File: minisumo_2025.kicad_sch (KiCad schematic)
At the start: 90 parts, among them J1 USB_C Connector, J10 DISTANCE_R90, J11 DISTANCE_R, J12 DISTANCE_RF, J13 DISTANCE_L90, J14 DISTANCE_L, J15 LINE_LEFT, J16 DISTANCE_LF, J2 SERVO, J3 START_MODULE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

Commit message: usb routing
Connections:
- net GPIO15 is gone; now on net DISTANCE_L: U3.8 (IO15)
- net GPIO16 is gone; now on net DISTANCE_L90: U3.9 (IO16)
- net GPIO4 is gone; now on net DISTANCE_R90: U3.4 (IO4)
- net GPIO5 is gone; now on net DISTANCE_R: U3.5 (IO5)
- net GPIO6 is gone; now on net DISTANCE_RF: U3.6 (IO6)
- net GPIO7 is gone; now on net DISTANCE_LF: U3.7 (IO7)
- net LINE_LEFT is gone; now on net GPIO8: R23.1, R24.2
- net LINE_RIGHT is gone; now on net GPIO18: R21.1, R22.2
- net SERVO_PWM is gone; now on net GPIO17: J2.3 (Pin_3)
- net DISTANCE_L: now also U5.2 (A2); no longer U5.8 (A6)
- net DISTANCE_L90: now also U5.1 (A1); no longer U5.9 (A7)
- net DISTANCE_L90_OUT: now also U5.20 (B1); no longer U5.12 (B7)
- net DISTANCE_LF: now also U5.3 (A3); no longer U5.7 (A5)
- net DISTANCE_LF_OUT: now also U5.18 (B3); no longer U5.14 (B5)
- net DISTANCE_L_OUT: now also U5.19 (B2); no longer U5.13 (B6)
- net DISTANCE_R: now also U5.8 (A6); no longer U5.2 (A2)
- net DISTANCE_R90: now also U5.9 (A7); no longer U5.1 (A1)
- net DISTANCE_R90_OUT: now also U5.12 (B7); no longer U5.20 (B1)
- net DISTANCE_RF: now also U5.7 (A5); no longer U5.3 (A3)
- net DISTANCE_RF_OUT: now also U5.14 (B5); no longer U5.18 (B3)
- net DISTANCE_R_OUT: now also U5.13 (B6); no longer U5.19 (B2)
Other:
- note added: "TODO: - maybe make clearance bigger between batt plane and gnd"
- note removed: "TODO: - DO NOT PLACE THE BIG CAPACITORS BETWEEN THE MOTORS, THEY ARE NOT NEEDED"
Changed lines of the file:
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@@
 		)
 	)
-	(text "TODO:\n - DO NOT PLACE THE BIG CAPACITORS BETWEEN THE MOTORS, THEY ARE NOT NEEDED\n\n\n"
+	(text "TODO:\n - maybe make clearance bigger between batt plane and gnd\n\n\n\n"
 		(exclude_from_sim no)
 		(at 290.322 22.606 0)
@@
 		)
 	)
-	(label "DISTANCE_L_OUT"
-		(at 87.63 229.87 180)
-		(effects
-			(font
-				(size 1.27 1.27)
-			)
-			(justify right bottom)
-		)
-	)
 	(label "ESP_EN"
 		(at 45.72 34.29 0)
@@
 		)
 	)
-	(label "DISTANCE_R"
-		(at 195.58 198.12 0)
-		(effects
-			(font
-				(size 1.27 1.27)
-			)
-			(justify left bottom)
-		)
-	)
 	(label "LINE_LEFT"
 		(at 142.24 267.97 180)
@@
 		)
 	)
+	(label "DISTANCE_R"
+		(at 125.73 229.87 0)
+		(effects
+			(font
+				(size 1.27 1.27)
+			)
+			(justify left bottom)
+		)
+	)
 	(label "START"
 		(at 120.65 92.71 0)
@@
 		)
 	)
-	(label "SERVO_PWM"
-		(at 228.6 195.58 0)
-		(effects
-			(font
-				(size 1.27 1.27)
-			)
-			(justify left bottom)
-		)
-	)
 	(label "GPIO7"
 		(at 322.58 64.77 180)
@@
 		)
 	)
+	(label "DISTANCE_L90_OUT"
+		(at 87.63 247.65 180)
+		(effects
+			(font
+				(size 1.27 1.27)
+			)
+			(justify right bottom)
+		)
+	)
 	(label "XSHUT"
 		(at 50.8 207.01 180)
@@
 		)
 	)
-	(label "DISTANCE_RF"
-		(at 125.73 242.57 0)
-		(effects
-			(font
-				(size 1.27 1.27)
-			)
-			(justify left bottom)
-		)
-	)
 	(label "IN2_1"
 		(at 34.29 149.86 0)
@@
 		)
 	)
-	(label "DISTANCE_R90"
-		(at 125.73 247.65 0)
+	(label "SERVO_PWM"
+		(at 360.68 59.69 0)
 		(effects
 			(font
@@
 		)
 	)
+	(label "DISTANCE_L90"
+		(at 360.68 57.15 0)
+		(effects
+			(font
+				(size 1.27 1.27)
+			)
+			(justify left bottom)
+		)
+	)
 	(label "GPIO13"
 		(at 55.88 72.39 180)
@@
 		)
 	)
-	(label "DISTANCE_RF_OUT"
-		(at 87.63 242.57 180)
-		(effects
-			(font
-				(size 1.27 1.27)
-			)
-			(justify right bottom)
+	(label "DISTANCE_L"
+		(at 360.68 54.61 0)
+		(effects
+			(font
+				(size 1.27 1.27)
+			)
+			(justify left bottom)
 		)
 	)
@@
 		)
 	)
-	(label "DISTANCE_LF"
-		(at 212.09 200.66 0)
+	(label "LINE_RIGHT"
+		(at 360.68 62.23 0)
 		(effects
 			(font
@@
 		)
 	)
-	(label "LINE_LEFT"
-		(at 212.09 203.2 0)
-		(effects
-			(font
-				(size 1.27 1.27)
-			)
-			(justify left bottom)
-		)
-	)
 	(label "MOTOR2_B"
 		(at 222.25 151.13 180)
@@
 		)
 	)
-	(label "DISTANCE_R90_OUT"
-		(at 87.63 247.65 180)
+	(label "DISTANCE_L_OUT"
+		(at 87.63 245.11 180)
 		(effects
 			(font
@@
 		)
 	)
+	(label "DISTANCE_RF"
+		(at 327.66 62.23 0)
+		(effects
+			(font
+				(size 1.27 1.27)
+			)
+			(justify left bottom)
+		)
+	)
 	(label "GPIO16"
 		(at 55.88 80.01 180)
@@
 		)
 	)
+	(label "DISTANCE_R"
+		(at 327.66 59.69 0)
+		(effects
+			(font
+				(size 1.27 1.27)
+			)
+			(justify left bottom)
+		)
+	)
 	(label "GPIO6"
 		(at 55.88 54.61 180)
@@
 		)
 	)
+	(label "DISTANCE_R90"
+		(at 327.66 57.15 0)
+		(effects
+			(font
+				(size 1.27 1.27)
+			)
+			(justify left bottom)
+		)
+	)
 	(label "DISTANCE_R_OUT"
 		(at 59.69 229.87 180)
@@
 		)
 	)
-	(label "DISTANCE_L90_OUT"
-		(at 87.63 227.33 180)
-		(effects
-			(font
-				(size 1.27 1.27)
-			)
-			(justify right bottom)
-		)
-	)
-	(label "DISTANCE_L"
-		(at 125.73 229.87 0)
-		(effects
-			(font
-				(size 1.27 1.27)
-			)
-			(justify left bottom)
+	(label "DISTANCE_LF_OUT"
+		(at 87.63 242.57 180)
+		(effects
+			(font
+				(size 1.27 1.27)
+			)
+			(justify right bottom)
 		)
 	)
@@
 		)
 	)
-	(label "DISTANCE_L90"
-		(at 125.73 227.33 0)
+	(label "LINE_LEFT"
+		(at 327.66 67.31 0)
 		(effects
 			(font
@@
 		)
 	)
+	(label "DISTANCE_RF_OUT"
+		(at 87.63 232.41 180)
+		(effects
+			(font
+				(size 1.27 1.27)
+			)
+			(justify right bottom)
+		)
+	)
 	(label "D+"
 		(at 104.14 49.53 0)
@@
 		)
 	)
+	(label "DISTANCE_L90"
+		(at 125.73 247.65 0)
+		(effects
+			(font
+				(size 1.27 1.27)
+			)
+			(justify left bottom)
+		)
+	)
 	(label "GPIO36"
 		(at 86.36 54.61 0)
@@
 		)
 	)
+	(label "DISTANCE_R_OUT"
+		(at 87.63 229.87 180)
+		(effects
+			(font
+				(size 1.27 1.27)
+			)
+			(justify right bottom)
+		)
+	)
 	(label "DISTANCE_RF_OUT"
 		(at 60.96 241.3 180)
@@
 		)
 	)
-	(label "DISTANCE_LF"
-		(at 125.73 232.41 0)
-		(effects
-			(font
-				(size 1.27 1.27)
-			)
-			(justify left bottom)
-		)
-	)
 	(label "GPIO14"
 		(at 55.88 74.93 180)
@@
 		)
 	)
-	(label "DISTANCE_R"
-		(at 125.73 245.11 0)
-		(effects
-			(font
-				(size 1.27 1.27)
-			)
-			(justify left bottom)
-		)
-	)
 	(label "GPIO13"
 		(at 322.58 80.01 180)
@@
 		)
 	)
-	(label "DISTANCE_R90"
-		(at 195.58 195.58 0)
-		(effects
-			(font
-				(size 1.27 1.27)
-			)
-			(justify left bottom)
-		)
-	)
-	(label "LINE_RIGHT"
-		(at 195.58 203.2 0)
+	(label "DISTANCE_LF"
+		(at 327.66 64.77 0)
 		(effects
 			(font
@@
 		)
 	)
+	(label "DISTANCE_LF"
+		(at 125.73 242.57 0)
+		(effects
+			(font
+				(size 1.27 1.27)
+			)
+			(justify left bottom)
+		)
+	)
+	(label "DISTANCE_L"
+		(at 125.73 245.11 0)
+		(effects
+			(font
+				(size 1.27 1.27)
+			)
+			(justify left bottom)
+		)
+	)
 	(label "START"
 		(at 228.6 198.12 0)
@@
 		)
 	)
-	(label "DISTANCE_L"
-		(at 212.09 198.12 0)
-		(effects
-			(font
-				(size 1.27 1.27)
-			)
-			(justify left bottom)
-		)
-	)
 	(label "DISTANCE_LF_OUT"
 		(at 60.96 275.59 180)
@@
 		)
 	)
-	(label "DISTANCE_L90"
-		(at 212.09 195.58 0)
-		(effects
-			(font
-				(size 1.27 1.27)
-			)
-			(justify left bottom)
-		)
-	)
 	(label "GPIO12"
 		(at 55.88 69.85 180)
@@
 		)
 	)
-	(label "DISTANCE_R_OUT"
-		(at 87.63 245.11 180)
-		(effects
-			(font
-				(size 1.27 1.27)
-			)
-			(justify right bottom)
-		)
-	)
 	(label "GPIO11"
 		(at 322.58 74.93 180)
@@
 		)
 	)
+	(label "DISTANCE_RF"
+		(at 125.73 232.41 0)
+		(effects
+			(font
+				(size 1.27 1.27)
+			)
+			(justify left bottom)
+		)
+	)
 	(label "GPIO18"
 		(at 355.6 62.23 180)
@@
 		)
 	)
+	(label "DISTANCE_R90_OUT"
+		(at 87.63 227.33 180)
+		(effects
+			(font
+				(size 1.27 1.27)
+			)
+			(justify right bottom)
+		)
+	)
+	(label "DISTANCE_R90"
+		(at 125.73 227.33 0)
+		(effects
+			(font
+				(size 1.27 1.27)
+			)
+			(justify left bottom)
+		)
+	)
 	(label "CCP_2"
 		(at 186.69 132.08 0)
@@
 		)
 	)
-	(label "DISTANCE_LF_OUT"
-		(at 87.63 232.41 180)
-		(effects
-			(font
-				(size 1.27 1.27)
-			)
-			(justify right bottom)
-		)
-	)
 	(label "GPIO35"
 		(at 86.36 52.07 0)
@@
 		(effects
 			(font
-				(size 1.27 1.27)
-			)
-			(justify left bottom)
-		)
-	)
-	(label "DISTANCE_RF"
-		(at 195.58 200.66 0)
-		(effects
-			(font

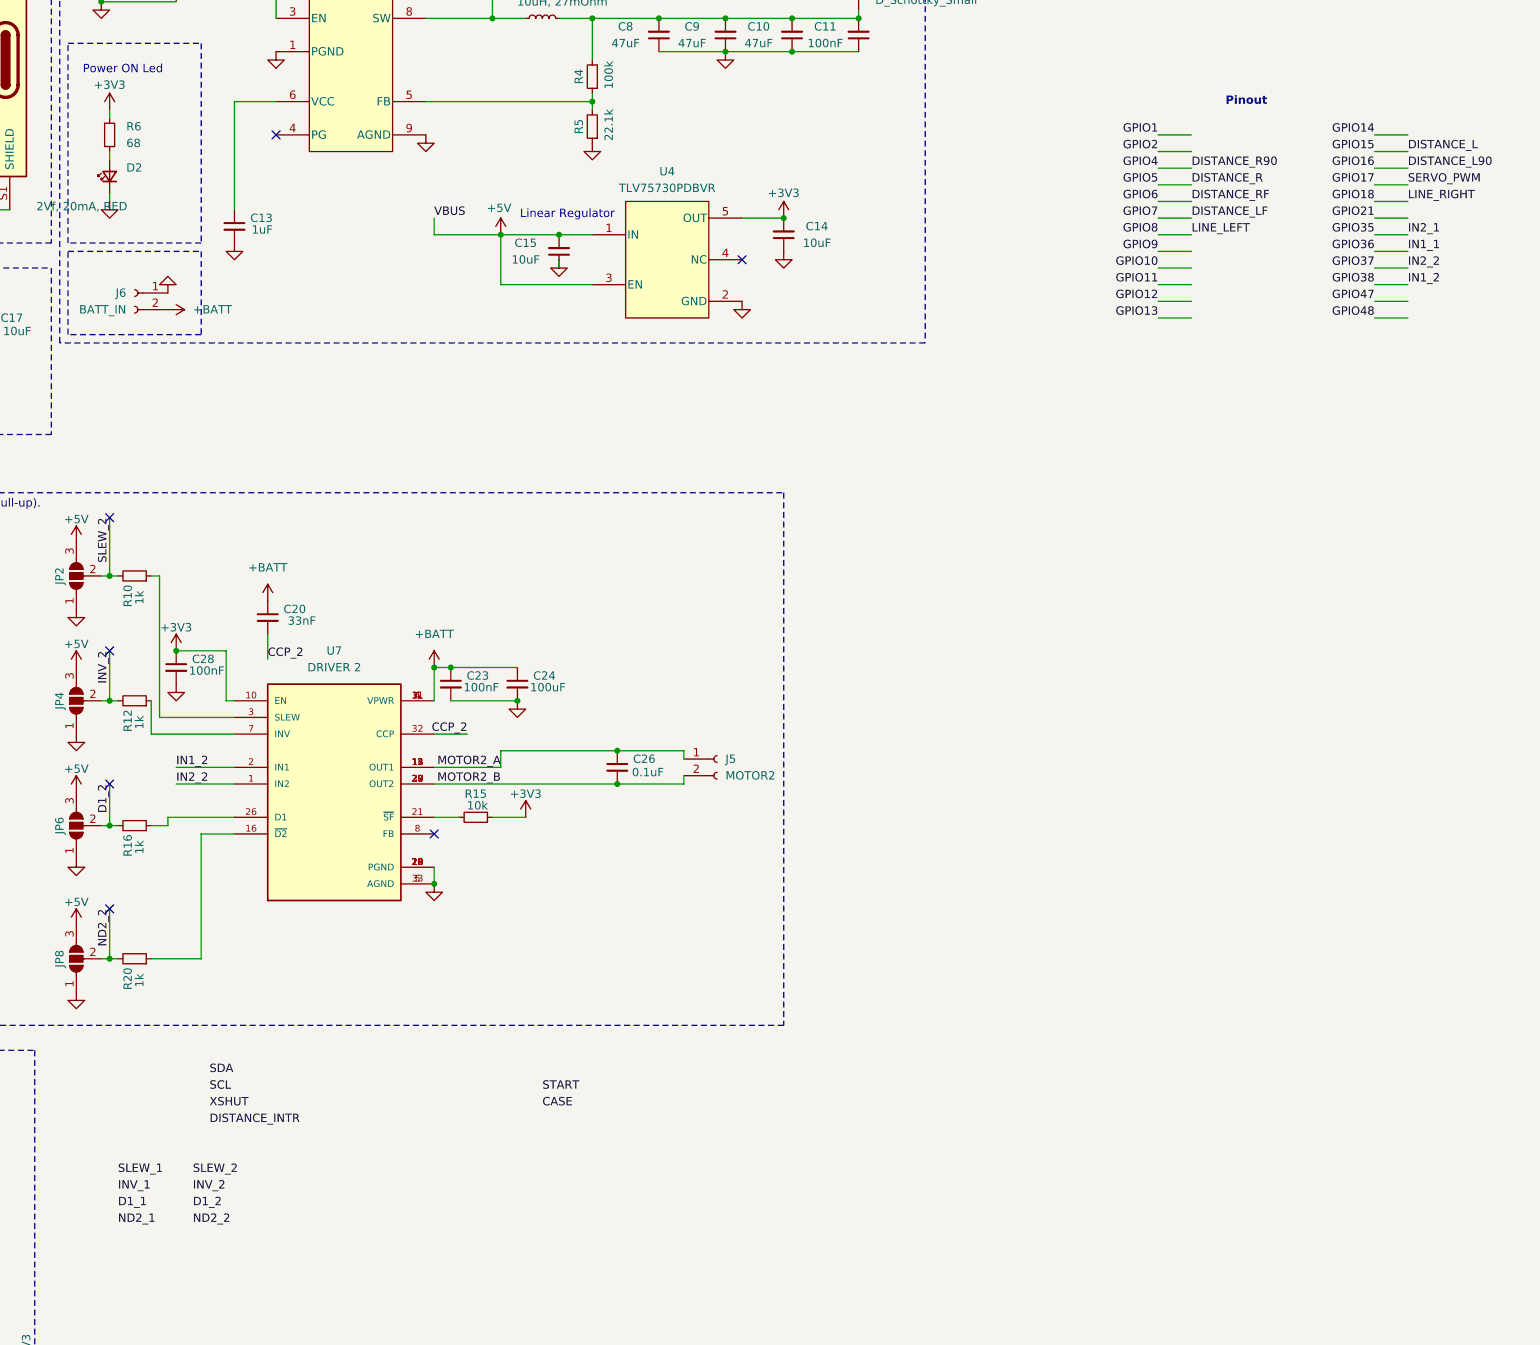
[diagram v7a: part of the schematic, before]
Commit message: finished overall routing
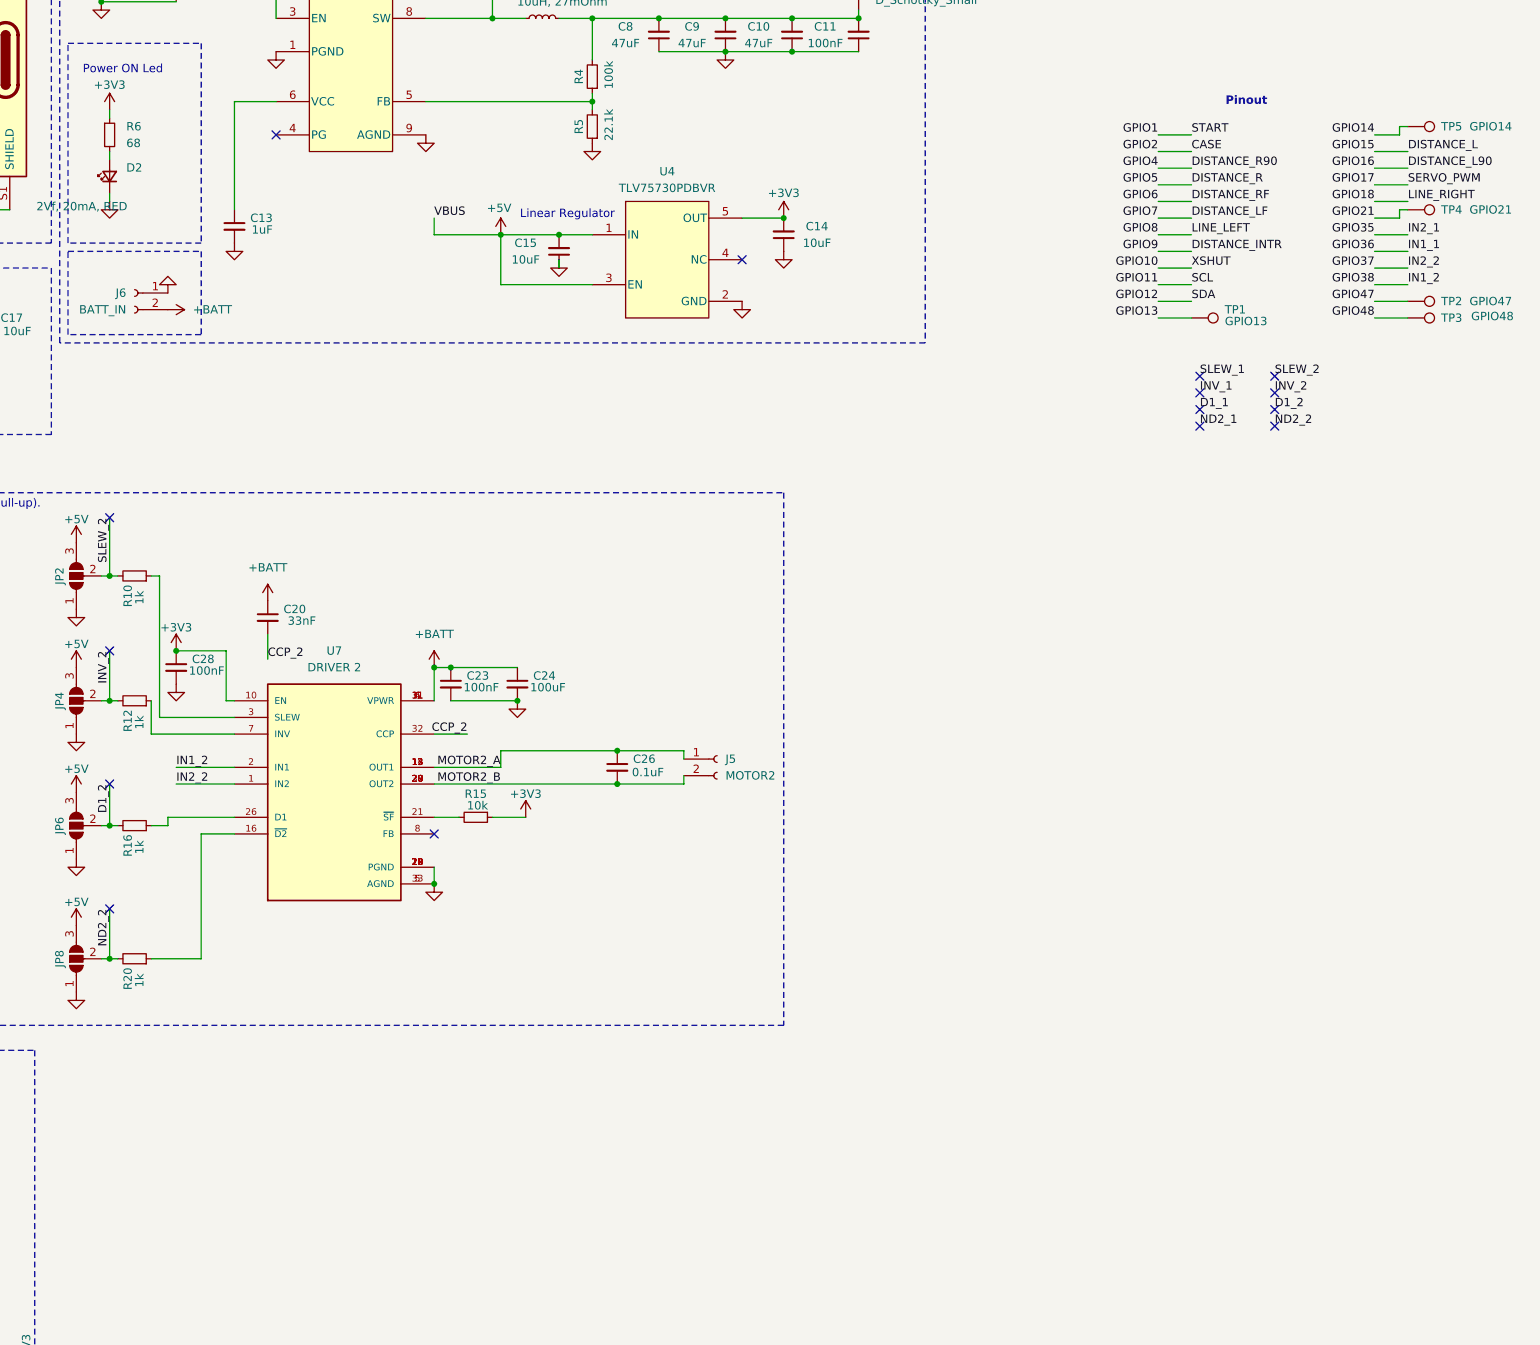
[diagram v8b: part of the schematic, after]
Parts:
- added TP1: GPIO13, TestPoint:TestPoint_Pad_1.5x1.5mm, symbol Connector:TestPoint
- added TP2: GPIO47, TestPoint:TestPoint_Pad_1.5x1.5mm, symbol Connector:TestPoint
- added TP3: GPIO48, TestPoint:TestPoint_Pad_1.5x1.5mm, symbol Connector:TestPoint
- added TP4: GPIO21, TestPoint:TestPoint_Pad_1.5x1.5mm, symbol Connector:TestPoint
- added TP5: GPIO14, TestPoint:TestPoint_Pad_1.5x1.5mm, symbol Connector:TestPoint
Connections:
- net GPIO2 is gone; now on net CASE: U3.38 (IO2)
- net GPIO9 is gone; now on net DISTANCE_INTR: U3.17 (IO9)
- net SCL is gone; now on net GPIO11: J8.4 (Pin_4)
- net SDA is gone; now on net GPIO12: J8.3 (Pin_3)
- net START is gone; now on net GPIO1: J3.3 (Pin_3)
- net XSHUT is gone; now on net GPIO10: J8.5 (Pin_5)
- net GPIO13: now also TP1.1
- net GPIO14: now also TP5.1
- net GPIO21: now also TP4.1
- net GPIO47: now also TP2.1
- net GPIO48: now also TP3.1
- no-connect marks 28 -> 36
